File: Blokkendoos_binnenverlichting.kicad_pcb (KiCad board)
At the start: 2 copper layers, 206.8 x 26 mm, 95 parts, among them J1 Conn_01x02, J10 Conn_01x04, J11 Conn_01x04, J12 Conn_01x04, J13 Conn_01x04, J2 Conn_02x11_Counter_Clockwise, J3 Conn_01x04, J4 Conn_01x02, J5 Conn_01x04, J6 Conn_01x02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

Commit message: Fixed all milestone 1 issues to date
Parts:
- added D1: LED, Pyth:MHT151CYCT, F.Cu at (51.8, 133.6)
- added D2: LED, Pyth:MHT151CYCT, F.Cu at (253.2, 133.6)
- added J14: Conn_01x04, TestPoint:TestPoint_Pad_1.0x1.0mm, F.Cu at (98.6, 127.3)
- added J15: Conn_01x04, TestPoint:TestPoint_Pad_1.0x1.0mm, F.Cu at (98.6, 125.0)
- added Q1: 21mtc-rescue_FDC6303N-mosfet_smd, Package_TO_SOT_SMD:SOT-363_SC-70-6_Handsoldering, F.Cu at (102.9, 125.7)
- added R7: R, Resistor_SMD:R_0805_2012Metric_Pad1.20x1.40mm_HandSolder, F.Cu at (103.9, 121.2)
- added R9: R, Resistor_SMD:R_0805_2012Metric_Pad1.20x1.40mm_HandSolder, F.Cu at (101.9, 121.2)
- D39, D41, D43, D45: value LED -> LS A67K
- D40, D44: value LED -> LY A67K
- D47, D48: footprint Pyth:MHT151CYCT -> Pyth:MHT151CYCT_dual_side
- moved R2 17.7 mm to (71.4, 119.9), turned to 180 degrees
- moved R3 9.91 mm to (71.4, 124.0), turned to 180 degrees
- moved D3 7.11 mm to (51.8, 119.9), turned to 90 degrees
- moved D6 7.11 mm to (253.2, 119.9), turned to 90 degrees
- moved D43 3.88 mm to (66.0, 122.5)
- moved D41 3.65 mm to (238.9, 122.5)
- moved D39 3.65 mm to (238.9, 131.5)
- moved D45 3.63 mm to (66.0, 131.5)
- moved R24 2.97 mm to (71.4, 121.9)
- moved R23 2.71 mm to (71.4, 126.0)
- moved R22 1.09 mm to (231.8, 120.0)
- moved R4 1.09 mm to (235.9, 120.0)
- moved R21 1.09 mm to (233.9, 120.0)
- moved J3 0.30 mm to (234.9, 116.6)
- moved R13 0.30 mm to (224.0, 117.0)
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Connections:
- D3 pad 1: /Aux2 -> Net-(D3-Pad1)
- D44 pad 1: /F0f -> /Aux5p
- D45 pad 1: /F0r -> /Aux6p
- D6 pad 1: /Aux3 -> Net-(D6-Pad1)
- J2 pad 17: unconnected-(J2-Pad17) -> /Aux5
- J2 pad 20: unconnected-(J2-Pad20) -> GND
- J2 pad 3: unconnected-(J2-Pad3) -> /Aux6
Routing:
- net /F0f: track 196.0 -> 129.4 mm, vias 5 -> 2
- net /F0r: track 187.4 -> 129.6 mm, vias 6 -> 4
- net GND: track 0.00 -> 44.8 mm
- net /Aux5p: track 0.00 -> 43.7 mm, vias 0 -> 2
- net /Aux6p: track 0.00 -> 37.6 mm
- net /Aux5: track 0.00 -> 30.8 mm, vias 0 -> 4
- net VPP: track 224.8 -> 202.1 mm
- net /Aux6: track 0.00 -> 21.7 mm
- net Net-(D3-Pad2): track 2.55 -> 19.3 mm
- net Net-(D43-Pad1): track 29.8 -> 17.7 mm
- net Net-(D3-Pad1): track 0.00 -> 11.6 mm
- net Net-(D6-Pad1): track 0.00 -> 11.4 mm
- net Net-(D4-Pad1): track 212.5 -> 222.5 mm
- net Net-(D4-Pad2): track 7.75 -> 15.0 mm, vias 0 -> 1
- net Net-(D39-Pad1): track 22.1 -> 16.2 mm
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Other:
- outline, holes or cut-outs redrawn
- board text added: "Aux5p"
- board text added: "Aux6p"
- board text added: "JLCJLCJLCJLC"

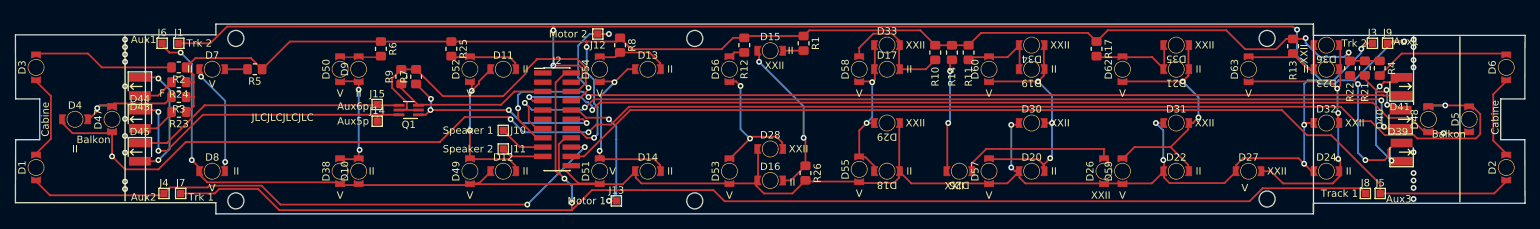
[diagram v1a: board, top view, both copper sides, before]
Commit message: Holes for motor wires
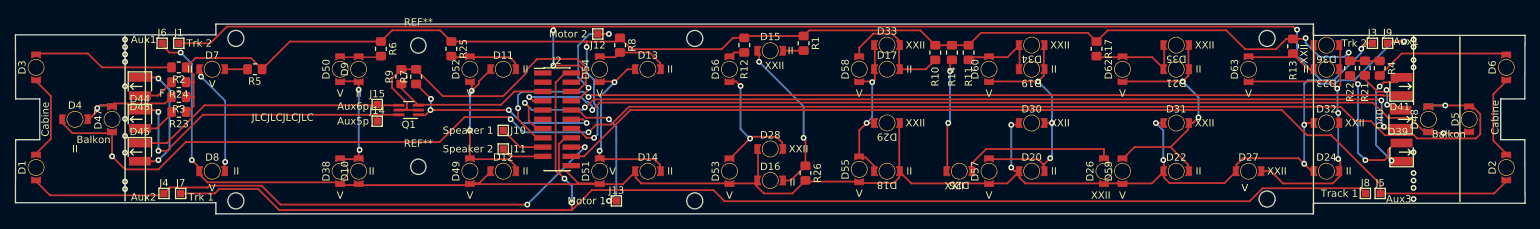
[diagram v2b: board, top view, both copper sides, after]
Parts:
- added REF**: MountingHole_2.1mm, MountingHole:MountingHole_2.1mm, F.Cu at (104.2, 133.5)
- added REF**: MountingHole_2.1mm, MountingHole:MountingHole_2.1mm, F.Cu at (104.2, 116.9)
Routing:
- net VPP: track 202.1 -> 203.4 mm
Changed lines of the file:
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@@
       ))
   )
+  (footprint "MountingHole:MountingHole_2.1mm" (layer "F.Cu")
+    (at 104.1908 133.5024)
+    (descr "Mounting Hole 2.1mm, no annular")
+    (tags "mounting hole 2.1mm no annular")
+    (attr exclude_from_pos_files exclude_from_bom)
+    (fp_text reference "REF**" (at 0 -3.2) (layer "F.SilkS")
+      (effects (font (size 1 1) (thickness 0.15)))
+    )
+    (fp_text value "MountingHole_2.1mm" (at 0 3.2) (layer "F.Fab")
+      (effects (font (size 1 1) (thickness 0.15)))
+    )
+    (fp_text user "${REFERENCE}" (at 0.3 0) (layer "F.Fab")
+      (effects (font (size 1 1) (thickness 0.15)))
+    )
+    (fp_circle (center 0 0) (end 2.1 0) (layer "Cmts.User") (width 0.15) (fill none))
+    (fp_circle (center 0 0) (end 2.35 0) (layer "F.CrtYd") (width 0.05) (fill none))
+    (pad "" np_thru_hole circle (at 0 0) (size 2.1 2.1) (drill 2.1) (layers *.Cu *.Mask))
+  )
   (footprint "Pyth:LED_Osram_LY_A64K" (layer "F.Cu")
     (at 238.9 122.5 90)
@@
       (primitives
         (gr_poly (pts
-            (xy -0.49 -0.32)
-            (xy -0.446 0)
-            (xy -0.49 0.32)
-            (xy -0.638 0.625)
             (xy 0.217 0.625)
-            (xy 0.217 -0.625)
+            (xy -0.638 0.625)
+            (xy -0.49 0.32)
+            (xy -0.446 0)
+            (xy -0.49 -0.32)
             (xy -0.638 -0.625)
+            (xy 0.217 -0.625)
           ) (width 0.1) (fill yes))
       ))
@@
       (primitives
         (gr_poly (pts
-            (xy -0.49 -0.32)
-            (xy -0.446 0)
-            (xy -0.49 0.32)
-            (xy -0.638 0.625)
             (xy 0.217 0.625)
-            (xy 0.217 -0.625)
+            (xy -0.638 0.625)
+            (xy -0.49 0.32)
+            (xy -0.446 0)
+            (xy -0.49 -0.32)
             (xy -0.638 -0.625)
+            (xy 0.217 -0.625)
           ) (width 0.1) (fill yes))
       ))
@@
       (net 15 "/Aux1") (pinfunction "Pin_1") (pintype "passive"))
   )
+  (footprint "MountingHole:MountingHole_2.1mm" (layer "F.Cu")
+    (at 104.1908 116.8908)
+    (descr "Mounting Hole 2.1mm, no annular")
+    (tags "mounting hole 2.1mm no annular")
+    (attr exclude_from_pos_files exclude_from_bom)
+    (fp_text reference "REF**" (at 0 -3.2) (layer "F.SilkS")
+      (effects (font (size 1 1) (thickness 0.15)))
+    )
+    (fp_text value "MountingHole_2.1mm" (at 0 3.2) (layer "F.Fab")
+      (effects (font (size 1 1) (thickness 0.15)))
+    )
+    (fp_text user "${REFERENCE}" (at 0.3 0) (layer "F.Fab")
+      (effects (font (size 1 1) (thickness 0.15)))
+    )
+    (fp_circle (center 0 0) (end 2.1 0) (layer "Cmts.User") (width 0.15) (fill none))
+    (fp_circle (center 0 0) (end 2.35 0) (layer "F.CrtYd") (width 0.05) (fill none))
+    (pad "" np_thru_hole circle (at 0 0) (size 2.1 2.1) (drill 2.1) (layers *.Cu *.Mask))
+  )
   (footprint "Resistor_SMD:R_0805_2012Metric_Pad1.20x1.40mm_HandSolder" (layer "F.Cu")
     (at 197.104 117.348 -90)
@@
   (segment (start 108.712 116.348) (end 127.238 116.348) (width 0.25) (layer "F.Cu") (net 25))
   (segment (start 179.578 116.856) (end 177.292 116.856) (width 0.25) (layer "F.Cu") (net 25))
-  (segment (start 99.06 116.348) (end 108.712 116.348) (width 0.25) (layer "F.Cu") (net 25))
   (segment (start 125.97 128.27) (end 127.24 129.54) (width 0.25) (layer "F.Cu") (net 25))
   (segment (start 223.0976 115.9924) (end 221.693479 117.396521) (width 0.25) (layer "F.Cu") (net 25))
@@
   (segment (start 217.472521 117.396521) (end 214.884 114.808) (width 0.25) (layer "F.Cu") (net 25))
   (segment (start 224.028 115.9924) (end 223.0976 115.9924) (width 0.25) (layer "F.Cu") (net 25))
+  (segment (start 99.06 116.348) (end 100.6 114.808) (width 0.25) (layer "F.Cu") (net 25))
   (segment (start 131.318 116.348) (end 131.826 115.84) (width 0.25) (layer "F.Cu") (net 25))
   (segment (start 157.74231 114.81569) (end 156.972 115.586) (width 0.25) (layer "F.Cu") (net 25))
@@
   (segment (start 214.884 114.808) (end 198.644 114.808) (width 0.25) (layer "F.Cu") (net 25))
   (segment (start 86.582 116.348) (end 99.06 116.348) (width 0.25) (layer "F.Cu") (net 25))
+  (segment (start 100.6 114.808) (end 107.172 114.808) (width 0.25) (layer "F.Cu") (net 25))
   (segment (start 172.96569 114.81569) (end 157.74231 114.81569) (width 0.25) (layer "F.Cu") (net 25))
   (segment (start 197.104 116.348) (end 195.9196 115.1636) (width 0.25) (layer "F.Cu") (net 25))
@@
   (segment (start 82.788 120.142) (end 81.264 118.618) (width 0.25) (layer "F.Cu") (net 25))
   (segment (start 72.374 123.952) (end 73.406 123.952) (width 0.25) (layer "F.Cu") (net 25))
+  (segment (start 107.172 114.808) (end 108.712 116.348) (width 0.25) (layer "F.Cu") (net 25))
   (segment (start 127.238 116.348) (end 131.318 116.348) (width 0.25) (layer "F.Cu") (net 25))
   (segment (start 133.382521 117.396521) (end 131.826 115.84) (width 0.25) (layer "F.Cu") (net 25))

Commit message: Removed plating on reverse mounted LED's, close #13
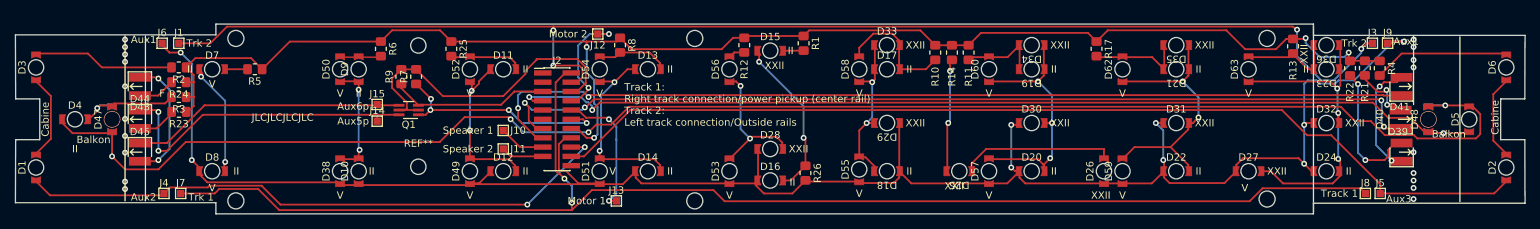
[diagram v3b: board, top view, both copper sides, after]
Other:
- board text added: "Track 1: Right track connection/power pickup (center rail) Track 2: Left track connection/Outside rails"
